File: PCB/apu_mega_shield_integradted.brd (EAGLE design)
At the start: 108 x 54.4 mm, 79 parts, among them IC1 74AHC573, IC10 DAC, IC11 IS62C1024AL, IC2 4050D, IC3 DS1307, IC4 LP298XS, IC5 S-SMP, IC6 S-DSP, IC7 LM2904, IC8 5x832 SRAM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

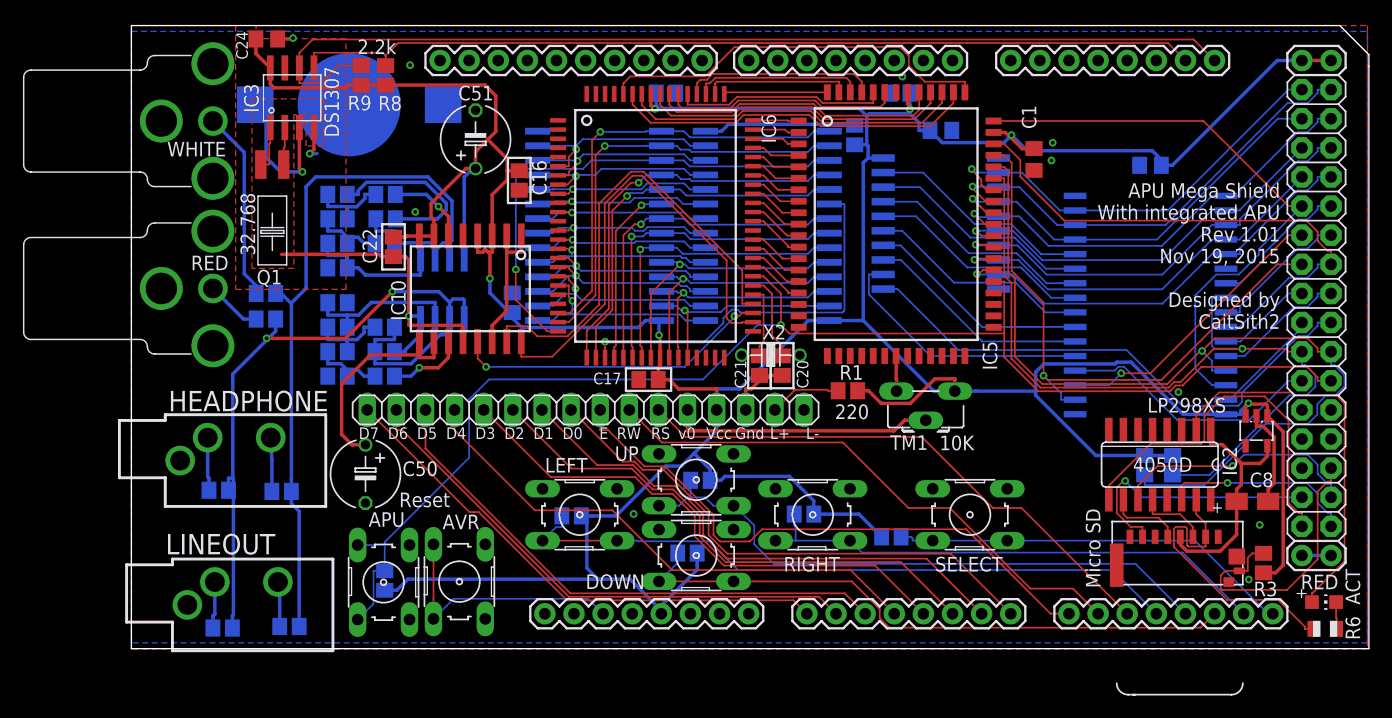
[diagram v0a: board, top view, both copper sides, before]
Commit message: R1 removed from PCB. It was supposed to be the current limiting resistor for the LCD backlight, however, the LCD module in use already has a current limiting resistor mounted right on that module.
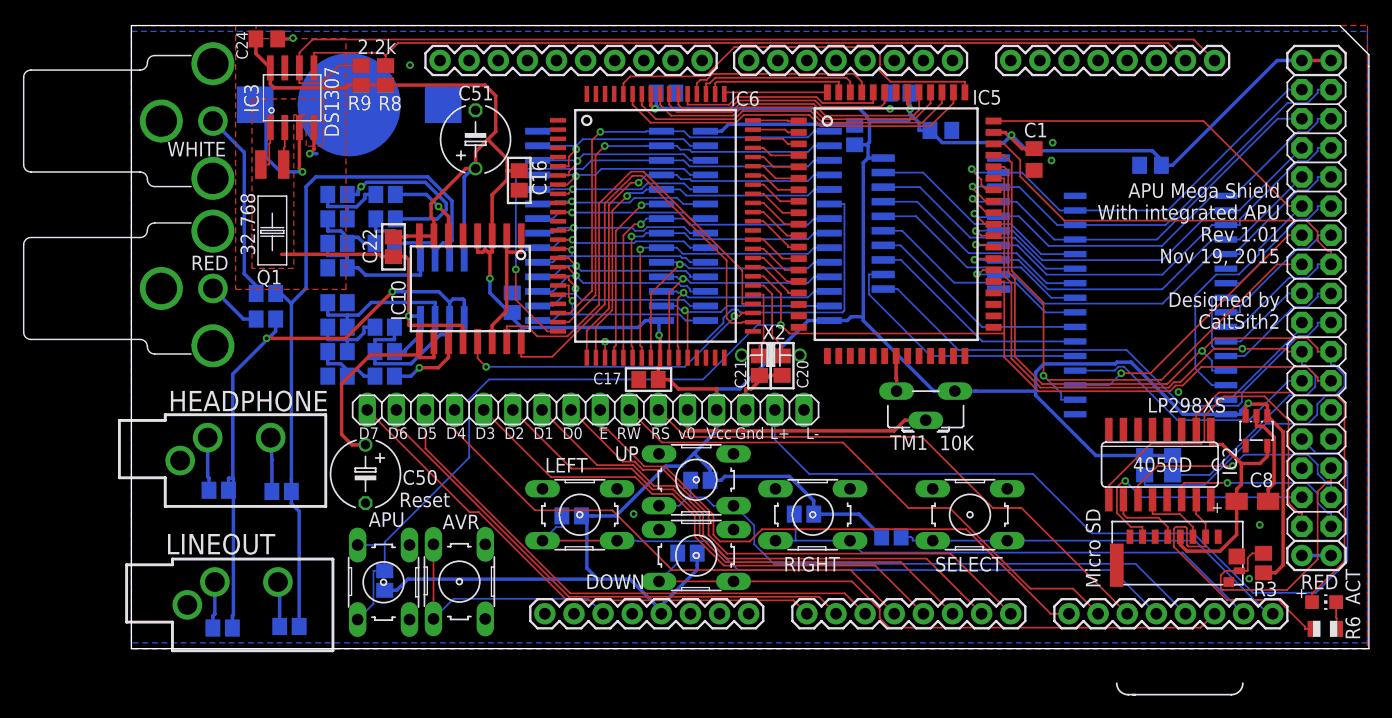
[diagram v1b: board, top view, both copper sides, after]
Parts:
- removed R1: 220, resistor:R0805
- C10, C13: value (none) -> 100pF
- C11, C14: value (none) -> 1800pF
- C12, C9: value (none) -> 1000pF
- C15, C16, C17, C18, C19, C22, C23: value (none) -> 0.1uF
- C20, C21: value (none) -> 3pF
- C50, C51: value (none) -> 47uF
- DOWN: value (none) -> DOWN
- LEFT: value (none) -> LEFT
- R16, R17, R18, R19, R20, R21: value (none) -> 22K
- R22, R23: value (none) -> 5.1K
- RIGHT: value (none) -> RIGHT
- SELECT: value (none) -> SELECT
- UP: value (none) -> UP
- X2: value (none) -> 24.576Mhz
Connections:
- removed net !MUTE: IC6.39
- removed net SMPCLK: IC6.78
- net N$14: now also U$6.46; no longer R1.2
- net VCC: no longer R1.1
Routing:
- net N$14: track 6.28 -> 72.6 mm
- net VCC: track 375.4 -> 364.9 mm

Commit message: Tweaked reset button layouts.  On the module version of the board, SD card connector and its supporting components moved.
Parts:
- moved C5 2.74 mm to (11.0, 1.94)
- moved C6 2.74 mm to (5.22, 1.80)
- moved R4 2.74 mm to (10.4, 13.7)
- moved R5 2.74 mm to (4.88, 13.8)
- moved U$3 2.74 mm to (6.84, 3.82)
- moved R2 2.64 mm to (20.3, 4.04), turned to 0 degrees
- moved APU 2.61 mm to (20.1, 3.98), turned to 180 degrees
- moved U$2 2.52 mm to (6.44, 16.5)
- moved AVR 2.27 mm to (29.9, 4.00), turned to 180 degrees
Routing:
- net N$1: track 22.6 -> 15.8 mm
- net GND: track 94.7 -> 97.1 mm
- net VCC: track 364.9 -> 366.3 mm
- net ALEFT: track 70.3 -> 71.5 mm
- net RST: track 120.5 -> 121.1 mm
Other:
- board text added: "APU Mega Shield With integrated APU Rev 1.01 Nov 25, 2015 Designed by CaitSith2"
- board text removed: "APU Mega Shield With integrated APU Rev 1.01 Nov 19, 2015 Designed by CaitSith2"

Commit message: Optimized layout a bit more.
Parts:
- moved R14 17.5 mm to (75.6, 24.5), flipped to the top, turned to 90 degrees
- moved R15 13.7 mm to (77.7, 24.5), flipped to the top, turned to 90 degrees
- turned R3 to 270 degrees
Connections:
- net A11: now also IC11.3; no longer IC11.2
- net A13: now also IC11.4; no longer IC11.3
- net A17: now also IC11.2; no longer IC11.4
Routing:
- net !WR: track 78.1 -> 52.6 mm
- net N$14: track 72.6 -> 47.8 mm
- net RST: track 121.1 -> 134.7 mm
- net VCC: track 366.3 -> 354.5 mm
- net CD: track 24.5 -> 16.4 mm
- net BUF_CS: track 25.7 -> 18.6 mm
- net DO: track 22.8 -> 16.1 mm
- net !RD: track 72.3 -> 67.6 mm
- net CLK: track 33.4 -> 29.8 mm, vias 0 -> 1
- net A7: track 23.2 -> 19.7 mm
- net GND: track 97.1 -> 94.5 mm, vias 12 -> 28
- net BUF_DI: track 6.09 -> 7.90 mm
- net +3V3: track 20.9 -> 22.6 mm
- net A17: track 23.3 -> 21.9 mm
- net BUF_LED: track 33.9 -> 35.0 mm
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
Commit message: Final revisions to the PCB design, hopefully. :)
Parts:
- C1, C2, C24, C7: device rcl:C0805 -> apu_pcb:C0805
- C3, C4, C5, C6: device resistor:C0805 -> apu_pcb:C0805
- R10, R11, R12, R13, R14, R15, R2, R3, R4, R5, R7, R8, R9: device resistor:R0805 -> adafruit:R0805
- R16, R17, R18, R19, R20, R21, R22, R23: device apu_pcb:R0805 -> adafruit:R0805
- moved C1 28.2 mm to (95.7, 20.1)
- moved R16 2.13 mm to (22.1, 25.9)
- moved R20 2.13 mm to (22.2, 37.5)
- moved R22 2.13 mm to (22.1, 23.8), turned to 0 degrees
- moved R23 2.13 mm to (22.2, 39.6), turned to 0 degrees
- moved C19 1.83 mm to (44.8, 48.5), turned to 0 degrees
- moved C2 1.52 mm to (88.9, 43.7)
- moved IC11 1.37 mm to (89.0, 31.3)
- moved IC9 0.63 mm to (55.5, 37.5)
- moved C50 0.61 mm to (20.4, 14.6)
- turned C10 to 180 degrees
- turned C9 to 0 degrees
- turned R17 to 180 degrees
- turned R18 to 180 degrees
- flipped X2 to the bottom, turned to 180 degrees
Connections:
- net N$14 renamed PWM
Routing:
- net GND: track 94.5 -> 38.5 mm, vias 28 -> 53
- net VCC: track 354.5 -> 390.3 mm
- net BCK: track 41.5 -> 21.6 mm, vias 0 -> 2
- net ARIGHT: track 66.7 -> 86.4 mm, vias 2 -> 0
- net SO: track 40.8 -> 25.7 mm, vias 0 -> 2
- net D13: track 43.9 -> 37.9 mm
- net N$15: track 12.7 -> 18.4 mm
- net A31: track 21.0 -> 25.9 mm
- net !WE: track 19.3 -> 24.2 mm
- net A26: track 22.5 -> 27.2 mm
- net A27: track 24.3 -> 27.3 mm
- net !WR: track 52.6 -> 49.6 mm
- net LCD_D4: track 46.7 -> 49.2 mm
- net ALEFT: track 71.5 -> 69.2 mm
- net LE: track 47.5 -> 45.2 mm
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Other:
- board text added: "APU Mega Shield With integrated APU Rev 1.03 Dec 12, 2015 Designed by CaitSith2"
- board text removed: "APU Mega Shield With integrated APU Rev 1.01 Nov 25, 2015 Designed by CaitSith2"
